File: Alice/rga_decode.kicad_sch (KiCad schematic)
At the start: 404 parts, among them Q333 NOT_OC, Q334 NOT_OC, Q335 NOT_OC, Q336 NOT_OC, Q337 NOT_OC, Q338 NOT_OC, Q339 NOT_OC, Q340 NOT_OC, Q341 NOT_OC, Q342 NOT_OC, Q343 NOT_OC, Q344 NOT_OC, Q345 NOT_OC, Q346 NOT_OC, Q347 NOT_OC, Q348 NOT_OC, Q349 NOT_OC, Q350 NOT_OC, Q351 NOT_OC, Q352 NOT_OC, Q353 NOT_OC, Q354 NOT_OC, Q355 NOT_OC, Q356 NOT_OC, Q357 NOT_OC, Q358 NOT_OC, Q359 NOT_OC, Q360 NOT_OC, Q361 NOT_OC, Q362 NOT_OC, Q363 NOT_OC, Q364 NOT_OC, Q365 NOT_OC, Q366 NOT_OC, Q367 NOT_OC, Q368 NOT_OC, Q369 NOT_OC, Q370 NOT_OC, Q371 NOT_OC, Q372 NOT_OC, Q373 NOT_OC, Q374 NOT_OC, Q375 NOT_OC, Q376 NOT_OC, Q377 NOT_OC, Q378 NOT_OC, Q379 NOT_OC, Q380 NOT_OC, Q381 NOT_OC, Q382 NOT_OC, Q383 NOT_OC, Q384 NOT_OC, Q385 NOT_OC, Q386 NOT_OC, Q387 NOT_OC, Q388 NOT_OC, Q389 NOT_OC, Q390 NOT_OC, Q391 NOT_OC, Q392 NOT_OC, Q393 NOT_OC, Q394 NOT_OC, Q395 NOT_OC, Q396 NOT_OC, Q397 NOT_OC, Q398 NOT_OC, Q399 NOT_OC, Q400 NOT_OC, Q401 NOT_OC, Q402 NOT_OC, Q403 NOT_OC, Q404 NOT_OC, Q405 NOT_OC, Q406 NOT_OC, Q407 NOT_OC, Q408 NOT_OC, Q409 NOT_OC, Q410 NOT_OC, Q411 NOT_OC, Q412 NOT_OC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

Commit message: Some refactoring : BEAMCON0 and BPLCON0 moved to the top sheet, CLOCKGEN added
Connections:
- net NRGB3: now reaches NOT_27.1, Q551.2, Q552.2, Q553.2, Q554.2, Q555.2, Q556.2, Q557.2, Q558.2, Q559.2, Q560.2, Q561.2, Q562.2, Q563.2, Q564.2, Q565.2, Q566.2
- net NRGB2: now reaches NOT_28.1, Q588.2, Q589.2, Q590.2, Q591.2, Q592.2, Q593.2, Q594.2, Q595.2, Q596.2, Q597.2, Q598.2, Q599.2, Q600.2, Q601.2, Q602.2, Q603.2, Q604.2, Q605.2, Q606.2
- net NRGB6: now reaches NOT_24.1, Q427.2, Q428.2, Q429.2, Q430.2, Q431.2, Q432.2, Q433.2, Q434.2, Q435.2, Q436.2, Q437.2, Q438.2, Q439.2, Q440.2, Q441.2, Q442.2, Q443.2, Q444.2, Q445.2, Q446.2, Q447.2, Q448.2, Q449.2, Q450.2, Q451.2, Q452.2
- net NRGB7: now reaches NOT_23.1, Q393.2, Q394.2, Q395.2, Q396.2, Q397.2, Q398.2, Q399.2, Q400.2, Q401.2, Q402.2, Q403.2, Q404.2, Q405.2, Q406.2, Q407.2, Q408.2, Q409.2, Q410.2, Q411.2, Q412.2
- net NRGB8: now reaches NOT_22.1, Q357.2, Q358.2, Q359.2, Q360.2, Q361.2, Q362.2, Q363.2, Q364.2, Q365.2, Q366.2, Q367.2, Q368.2, Q369.2, Q370.2, Q371.2, Q372.2
- net NRGB4: now reaches NOT_26.1, Q516.2, Q517.2, Q518.2, Q519.2, Q520.2, Q521.2, Q522.2, Q523.2, Q524.2, Q525.2, Q526.2, Q527.2, Q528.2
- net NRGB1: now reaches NOT_29.1, Q627.2, Q628.2, Q629.2, Q630.2, Q631.2, Q632.2, Q633.2, Q634.2, Q635.2, Q636.2, Q637.2, Q638.2, Q639.2, Q640.2, Q641.2, Q642.2, Q643.2, Q644.2, Q645.2, Q646.2
- net NRGB5: now reaches NOT_25.1, Q482.2, Q483.2, Q484.2, Q485.2, Q486.2, Q487.2, Q488.2, Q489.2, Q490.2
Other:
- moved on the sheet: CTL_DEMUX_1, POS_DEMUX_1

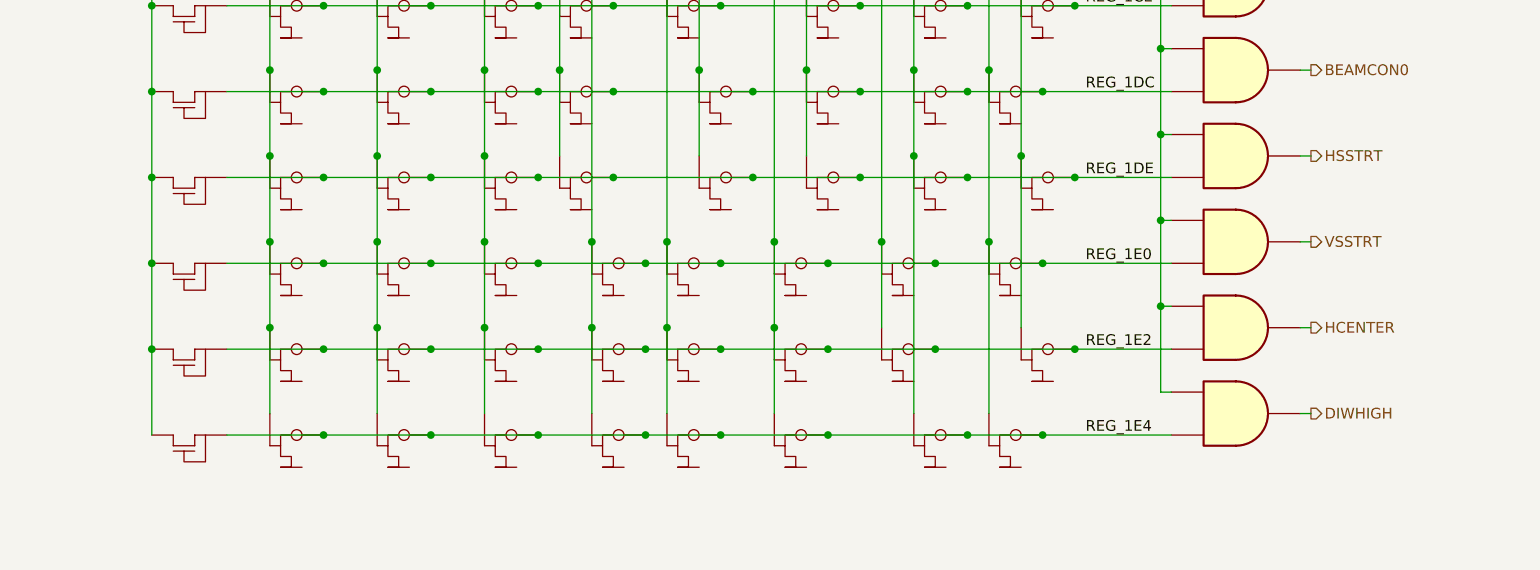
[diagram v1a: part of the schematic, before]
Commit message: BPLCON0 and FMODE registers added
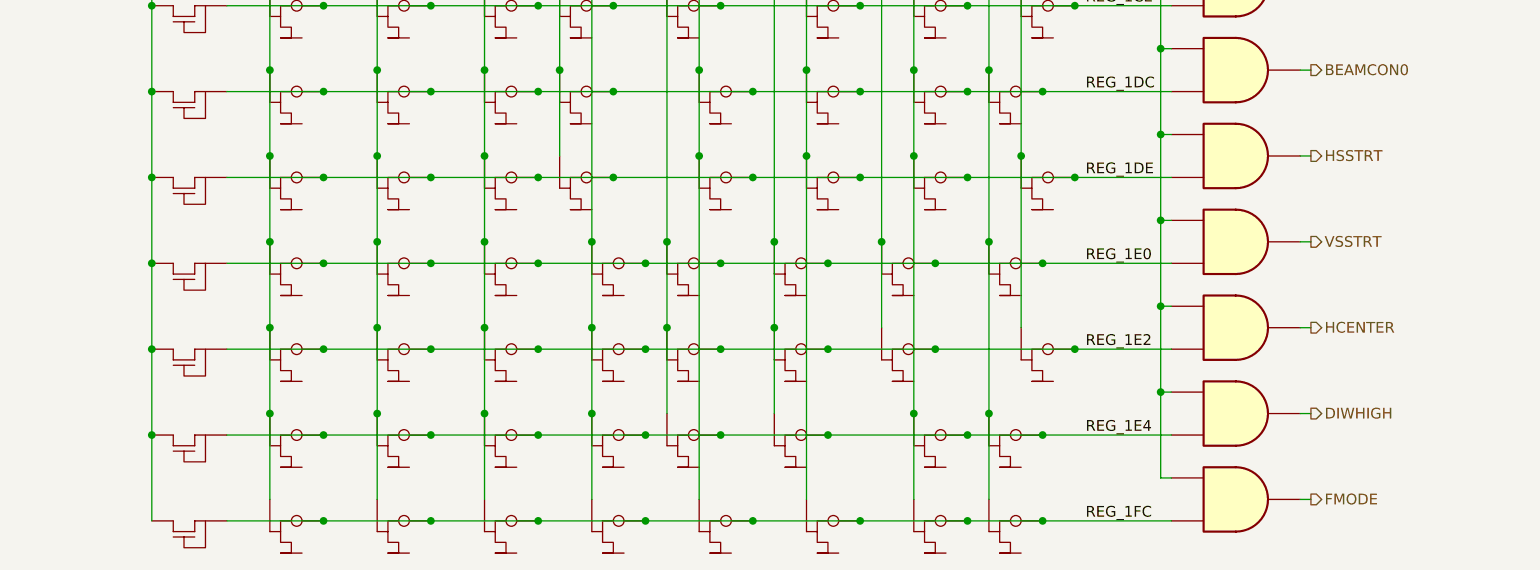
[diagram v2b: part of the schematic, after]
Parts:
- added AND_99: AND2, symbol NMOS:AND2
- added Q677, Q678, Q679, Q680, Q681, Q682, Q683, Q684: NOT_OC, symbol NMOS:NOT_OC
- added R84: PULLUP, symbol NMOS:PULLUP
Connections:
- net NRGB2: now also Q683.2
- net NRGB3: now also Q682.2
- net NRGB4: now also Q681.2
- net NRGB5: now also Q680.2
- net NRGB6: now also Q679.2
- net NRGB7: now also Q678.2
- net NRGB8: now also Q677.2
- net PHI2: now also AND_99.2
- net RGB1: now also Q684.2
- net VCC: now also R84.1 (S)
- new net FMODE: AND_99.1
- new net REG_1FC: AND_99.3, Q677.1, Q678.1, Q679.1, Q680.1, Q681.1, Q682.1, Q683.1, Q684.1, R84.3 (D)

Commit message: Copper DMA done
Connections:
- net PHI2: no longer AND_66.2, AND_67.2
- net VCC: now also AND_66.2, AND_67.2
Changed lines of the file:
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@@
   (junction (at 121.92 121.92) (diameter 0) (color 0 0 0 0)
   )
-  (junction (at 173.99 228.6) (diameter 0) (color 0 0 0 0)
-  )
   (junction (at 77.47 129.54) (diameter 0) (color 0 0 0 0)
   )
@@
   (junction (at 71.12 162.56) (diameter 0) (color 0 0 0 0)
   )
-  (junction (at 173.99 238.76) (diameter 0) (color 0 0 0 0)
-  )
   (junction (at 121.92 350.52) (diameter 0) (color 0 0 0 0)
   )
@@
     (stroke (width 0) (type default) (color 0 0 0 0))
   )
-  (wire (pts (xy 173.99 228.6) (xy 173.99 238.76))
-    (stroke (width 0) (type default) (color 0 0 0 0))
-  )
   (wire (pts (xy 232.41 303.53) (xy 220.98 303.53))
     (stroke (width 0) (type default) (color 0 0 0 0))
@@
     (stroke (width 0) (type default) (color 0 0 0 0))
   )
-  (wire (pts (xy 173.99 218.44) (xy 173.99 228.6))
-    (stroke (width 0) (type default) (color 0 0 0 0))
-  )
   (wire (pts (xy 71.12 172.72) (xy 83.82 172.72))
     (stroke (width 0) (type default) (color 0 0 0 0))
@@
     (stroke (width 0) (type default) (color 0 0 0 0))
   )
+  (wire (pts (xy 171.45 228.6) (xy 175.26 228.6))
+    (stroke (width 0) (type default) (color 0 0 0 0))
+  )
   (wire (pts (xy 175.26 386.08) (xy 173.99 386.08))
     (stroke (width 0) (type default) (color 0 0 0 0))
@@
     (stroke (width 0) (type default) (color 0 0 0 0))
   )
-  (wire (pts (xy 173.99 238.76) (xy 173.99 248.92))
+  (wire (pts (xy 173.99 218.44) (xy 173.99 248.92))
     (stroke (width 0) (type default) (color 0 0 0 0))
   )
@@
     (stroke (width 0) (type default) (color 0 0 0 0))
   )
-  (wire (pts (xy 175.26 238.76) (xy 173.99 238.76))
-    (stroke (width 0) (type default) (color 0 0 0 0))
-  )
   (wire (pts (xy 128.27 368.3) (xy 128.27 378.46))
     (stroke (width 0) (type default) (color 0 0 0 0))
@@
     (stroke (width 0) (type default) (color 0 0 0 0))
   )
+  (wire (pts (xy 171.45 238.76) (xy 175.26 238.76))
+    (stroke (width 0) (type default) (color 0 0 0 0))
+  )
   (wire (pts (xy 125.73 203.2) (xy 134.62 203.2))
     (stroke (width 0) (type default) (color 0 0 0 0))
@@
     (stroke (width 0) (type default) (color 0 0 0 0))
   )
-  (wire (pts (xy 175.26 228.6) (xy 173.99 228.6))
-    (stroke (width 0) (type default) (color 0 0 0 0))
-  )
   (bus (pts (xy 234.95 323.85) (xy 234.95 326.39))
     (stroke (width 0) (type default) (color 0 0 0 0))
@@
     (pin "2")
   )
+  (symbol (lib_id "power:VCC") (at 171.45 238.76 90) (unit 1)
+    (in_bom yes) (on_board yes)
+    (property "Reference" "#PWR0146" (id 0) (at 175.26 238.76 0)
+      (effects (font (size 1.27 1.27)) hide)
+    )
+    (property "Value" "VCC" (id 1) (at 168.275 239.239 90)
+      (effects (font (size 1.27 1.27)) (justify left))
+    )
+    (property "Footprint" "" (id 2) (at 171.45 238.76 0)
+      (effects (font (size 1.27 1.27)) hide)
+    )
+    (property "Datasheet" "" (id 3) (at 171.45 238.76 0)
+      (effects (font (size 1.27 1.27)) hide)
+    )
+    (pin "1")
+  )
   (symbol (lib_id "NMOS:NOT_OC") (at 115.57 82.55 0) (unit 1)
     (in_bom yes) (on_board yes) (fields_autoplaced)
@@
     (pin "2")
   )
+  (symbol (lib_id "power:VCC") (at 171.45 228.6 90) (unit 1)
+    (in_bom yes) (on_board yes)
+    (property "Reference" "#PWR0145" (id 0) (at 175.26 228.6 0)
+      (effects (font (size 1.27 1.27)) hide)
+    )
+    (property "Value" "VCC" (id 1) (at 168.275 229.079 90)
+      (effects (font (size 1.27 1.27)) (justify left))
+    )
+    (property "Footprint" "" (id 2) (at 171.45 228.6 0)
+      (effects (font (size 1.27 1.27)) hide)
+    )
+    (property "Datasheet" "" (id 3) (at 171.45 228.6 0)
+      (effects (font (size 1.27 1.27)) hide)
+    )
+    (pin "1")
+  )
   (symbol (lib_id "NMOS:NOT_OC") (at 77.47 214.63 0) (unit 1)
